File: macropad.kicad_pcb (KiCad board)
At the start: 2 copper layers, 187.7 x 88 mm, 79 parts, among them J1 SWD, J10 Keyboard 1, J11 Keyboard 1, J12 Keyboard 2, J13 Keyboard 2, J14 Keyboard 2, J15 Conn_01x12_Socket, J16 Conn_01x12_Pin, J2 Conn_01x12_Pin, J3 Conn_01x12_Socket, J4 Keyboard 1, J5 UART, J6 RS485, J7 Extra, J8 USB_A, J9 CAN, Q1 PNP, SW1 SW_Push, SW10 Reset, SW11 Reset, SW2 SW_Push, SW3 SW_Push, SW4 SW_Push, SW5 SW_Push, SW6 SW_Push, U1 AP62250WU, U2 STM32F042K6Tx, U3 MAX490E, U4 MCP2551-I-SN

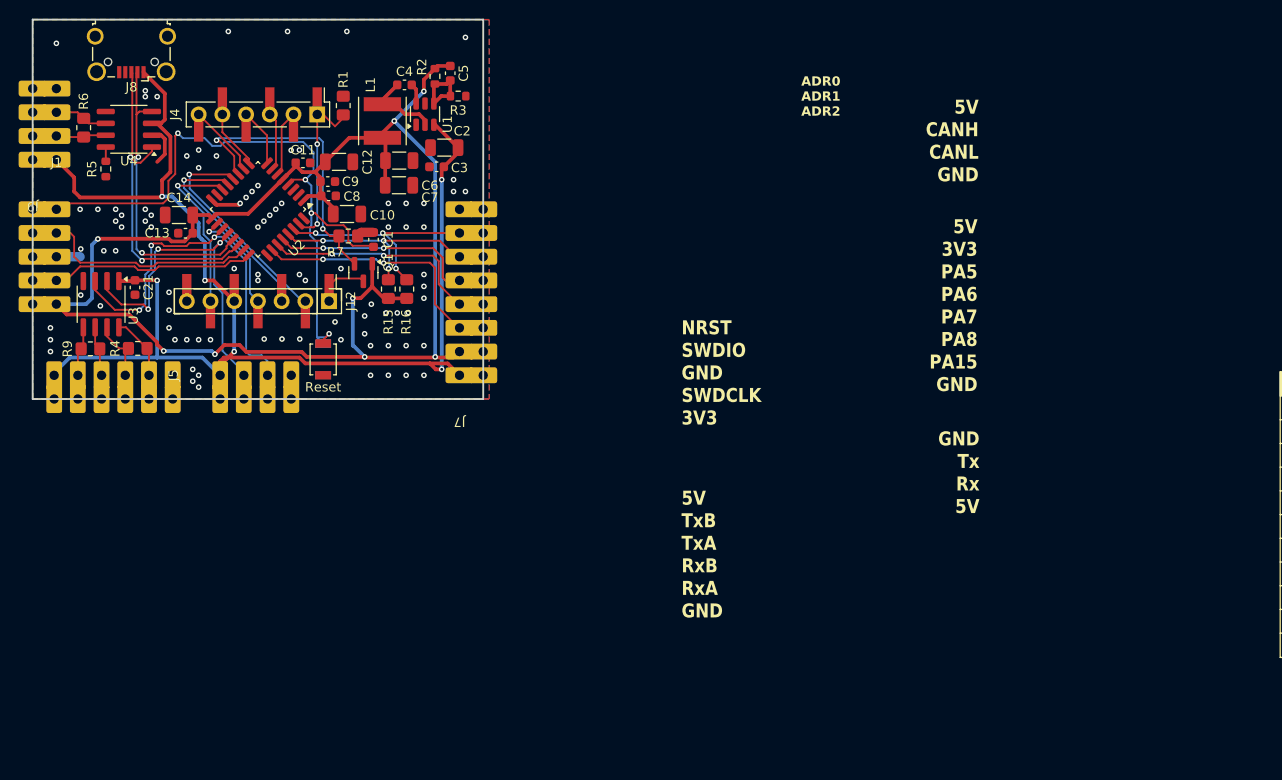
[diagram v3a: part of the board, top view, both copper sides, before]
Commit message: - fixed error in transistor circuit - fixed orientation of silkscreen text - DRC: Okay
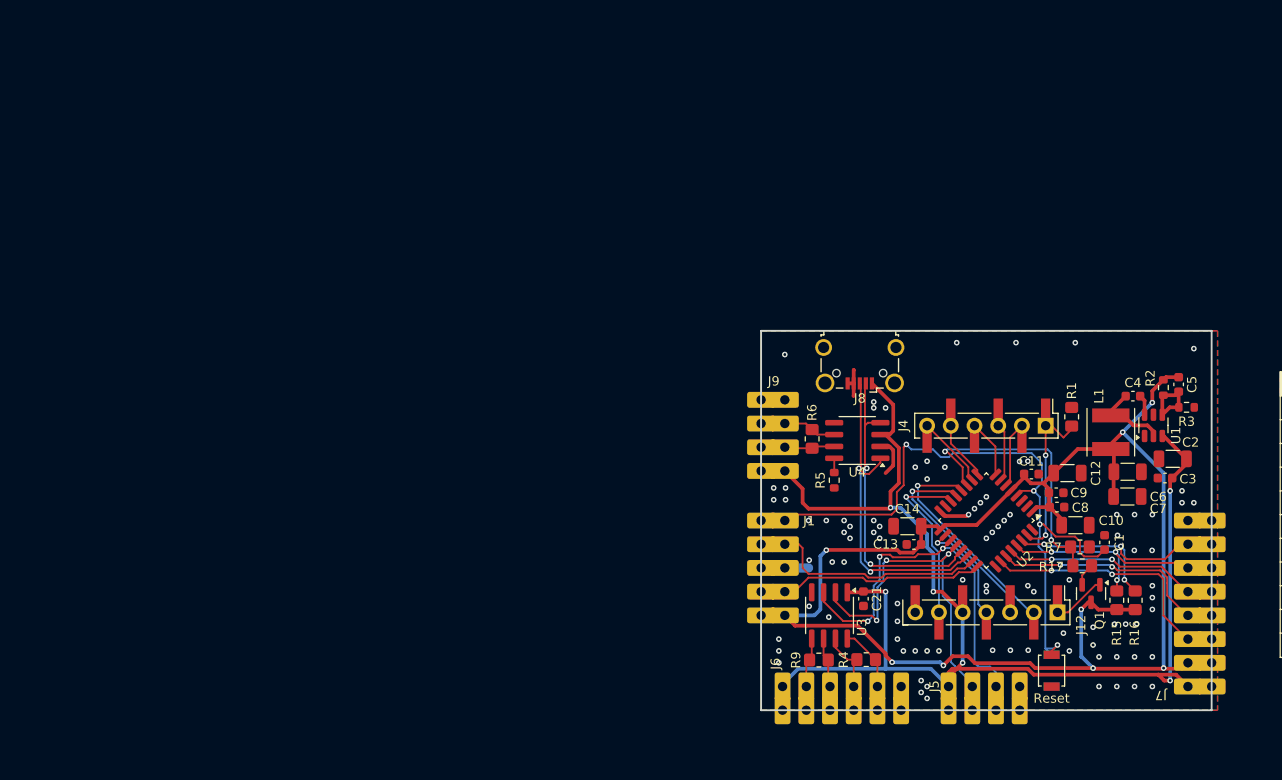
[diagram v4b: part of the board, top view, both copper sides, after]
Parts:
- added R17: 1k, Resistor_SMD:R_0805_2012Metric_Pad1.20x1.40mm_HandSolder, F.Cu at (126.3, 104.1)
- moved Q1 85.2 mm to (127.2, 107.1)
- moved R7 85.2 mm to (126.1, 102.1)
- moved C4 84.8 mm to (131.7, 86.0)
- moved J7 84.8 mm to (137.6, 117.1)
- moved R2 84.8 mm to (135.0, 85.0)
- moved U1 84.8 mm to (133.9, 89.1)
- moved C11 84.8 mm to (120.9, 94.3)
- moved C13 84.8 mm to (108.3, 101.9)
- moved C14 84.8 mm to (107.6, 99.9)
- moved C21 84.8 mm to (102.9, 107.7)
- moved C5 84.8 mm to (136.6, 84.7)
- moved C7 84.8 mm to (131.1, 96.7)
- moved C8 84.8 mm to (123.6, 97.9)
- moved J1 84.8 mm to (94.4, 99.3)
- moved J11 84.8 mm to (122.4, 89.1)
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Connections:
- Q1 pad 1: VDD -> GRP1
- Q1 pad 3: GRP1 -> VDD
- R7 pad 2: Net-(Q1-B) -> Net-(U2-PA5)
- U2 pad 11: Net-(Q1-B) -> Net-(U2-PA5)
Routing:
- net Net-(U2-PA5): track 0.00 -> 30.3 mm, vias 0 -> 2
- net Net-(Q1-B): track 31.9 -> 2.45 mm, vias 2 -> 0
- net VDD: track 163.1 -> 160.3 mm
- net GRP1: track 5.62 -> 7.26 mm
- net VSS: track 12.7 -> 14.3 mm, vias 89 -> 92
- net PB5: track 22.0 -> 20.7 mm
- net PB7: track 24.3 -> 25.2 mm
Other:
- board size 187.7 x 88 mm -> 109.7 x 70 mm
- board text added: "*CAN*"
- board text added: "*Extra* GND PB7 SDA PB6 SCL PB5 PB4 PB3 3V3 5V"
- board text added: "*PRG* NRST SWDIO GND SWDCLK 3V3"
- board text added: "*RS485*"
- board text added: "*UART*"
- board text added: "GND RxA RxB TxA TxB 5V"
- board text removed: "5V 3V3 PA5 PA6 PA7 PA8 PA15 GND"
- board text removed: "5V TxB TxA RxB RxA GND"
- board text removed: "ADR0 ADR1 ADR2"
- board text removed: "NRST SWDIO GND SWDCLK 3V3"

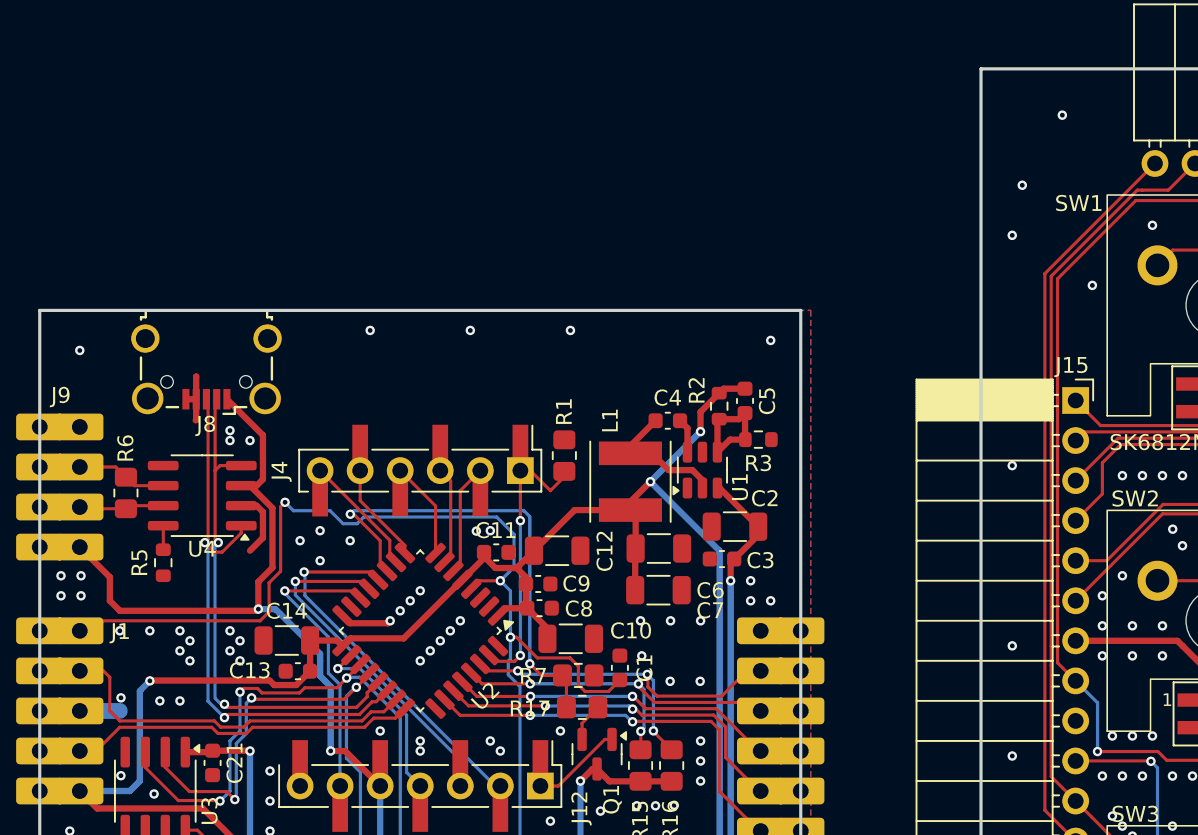
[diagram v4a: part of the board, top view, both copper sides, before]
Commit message: - Moved component name to silkscreen - Added version notation to boards
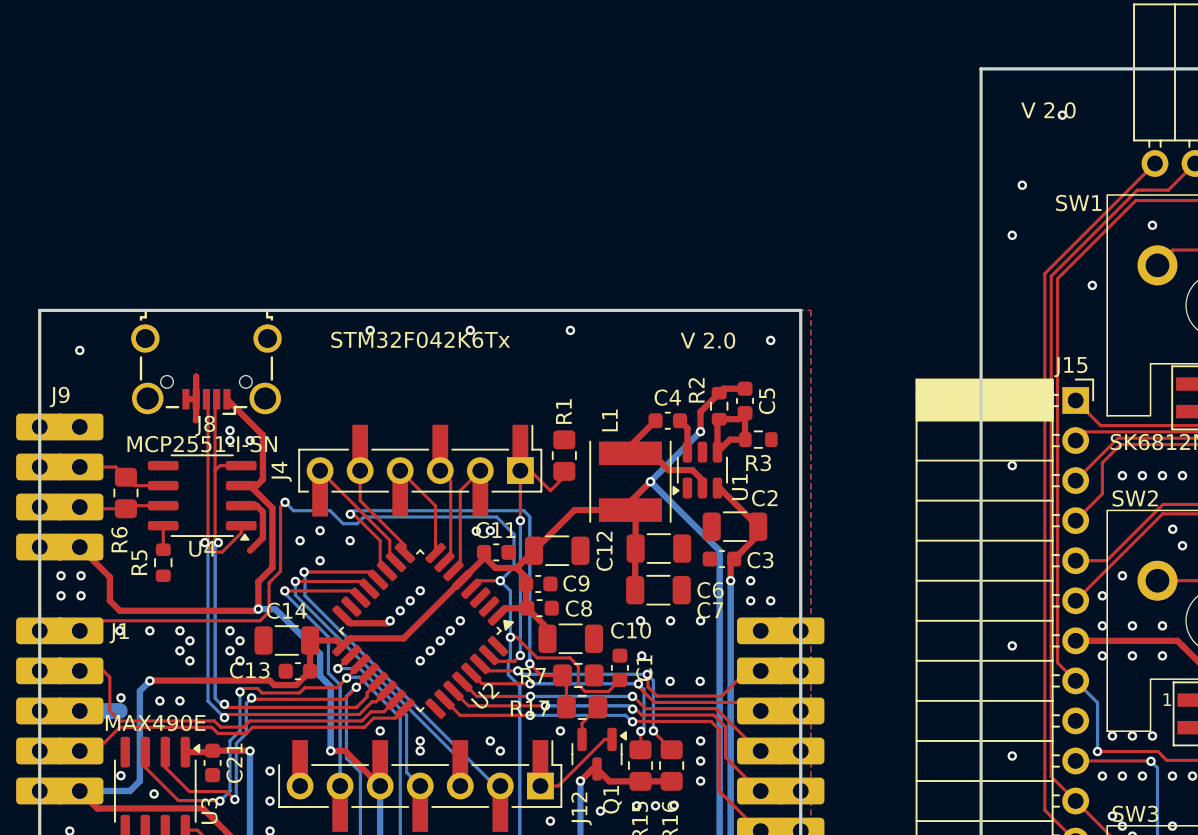
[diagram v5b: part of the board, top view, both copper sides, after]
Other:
- board text added: "V 2.0"
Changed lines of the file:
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@@
 		(allow_soldermask_bridges_in_footprints no)
 		(tenting front back)
-		(grid_origin 13.88 45.635)
+		(grid_origin 91.906177 78.971512)
 		(pcbplotparams
 			(layerselection 0x00000000_00000000_55555555_5755f5ff)
@@
 		(tags "resistor handsolder")
 		(property "Reference" "R6"
-			(at -2.829818 0 90)
+			(at 2.981145 0.374912 90)
 			(layer "F.SilkS")
 			(effects
@@
 		)
 		(property "Value" "STM32F042K6Tx"
-			(at 0 5.88 45)
-			(layer "F.Fab")
+			(at -13.021371 13.021371 0)
+			(layer "F.SilkS")
 			(effects
 				(font
@@
 		)
 		(property "Value" "MAX490E"
-			(at 0 3.4 90)
-			(layer "F.Fab")
+			(at -4.285371 0 180)
+			(layer "F.SilkS")
 			(effects
 				(font
@@
 		)
 		(property "Value" "MCP2551-I-SN"
-			(at 0 3.4 0)
-			(layer "F.Fab")
+			(at 0 3.231435 180)
+			(layer "F.SilkS")
 			(effects
 				(font
@@
 		(layer "Edge.Cuts")
 	)
+	(gr_text "V 2.0"
+		(at 154.136177 66.906512 0)
+		(layer "F.SilkS")
+		(effects
+			(font
+				(size 1 1)
+				(thickness 0.15)
+			)
+			(justify left bottom)
+		)
+	)
+	(gr_text "V 2.0"
+		(at 132.546177 81.511512 0)
+		(layer "F.SilkS")
+		(effects
+			(font
+				(size 1 1)
+				(thickness 0.15)
+			)
+			(justify left bottom)
+		)
+	)
 	(gr_text "\n5V\nCANH\nCANL\nGND"

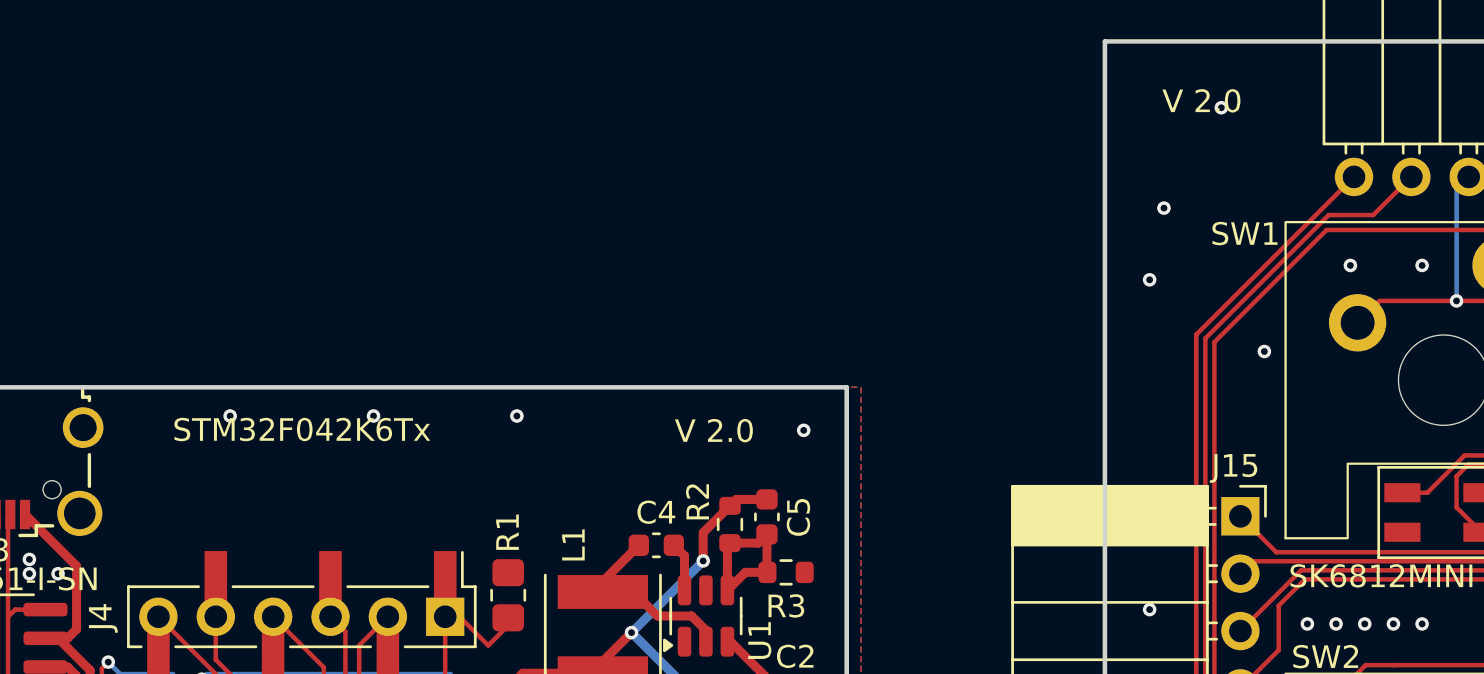
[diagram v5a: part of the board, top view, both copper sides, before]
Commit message: - Added missing library files to git - Added logo to silkscreen - ERC: Okay
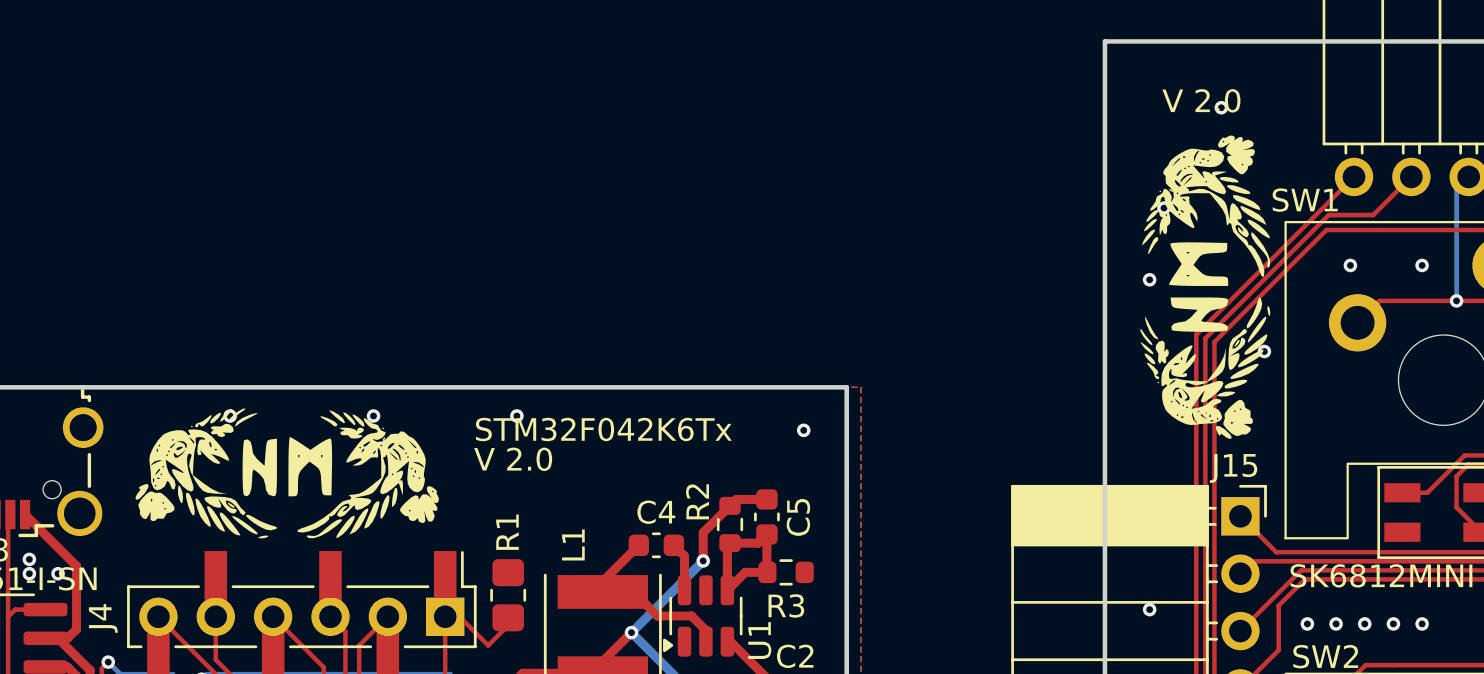
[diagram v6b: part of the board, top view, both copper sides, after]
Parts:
- added G***: LOGO, LOGO, F.Cu at (115.4, 82.8)
- added G***: LOGO, LOGO, F.Cu at (156.0, 74.5)
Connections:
- net USART1_RX renamed USART1_Rx
- net USART1_TX renamed USART1_Tx

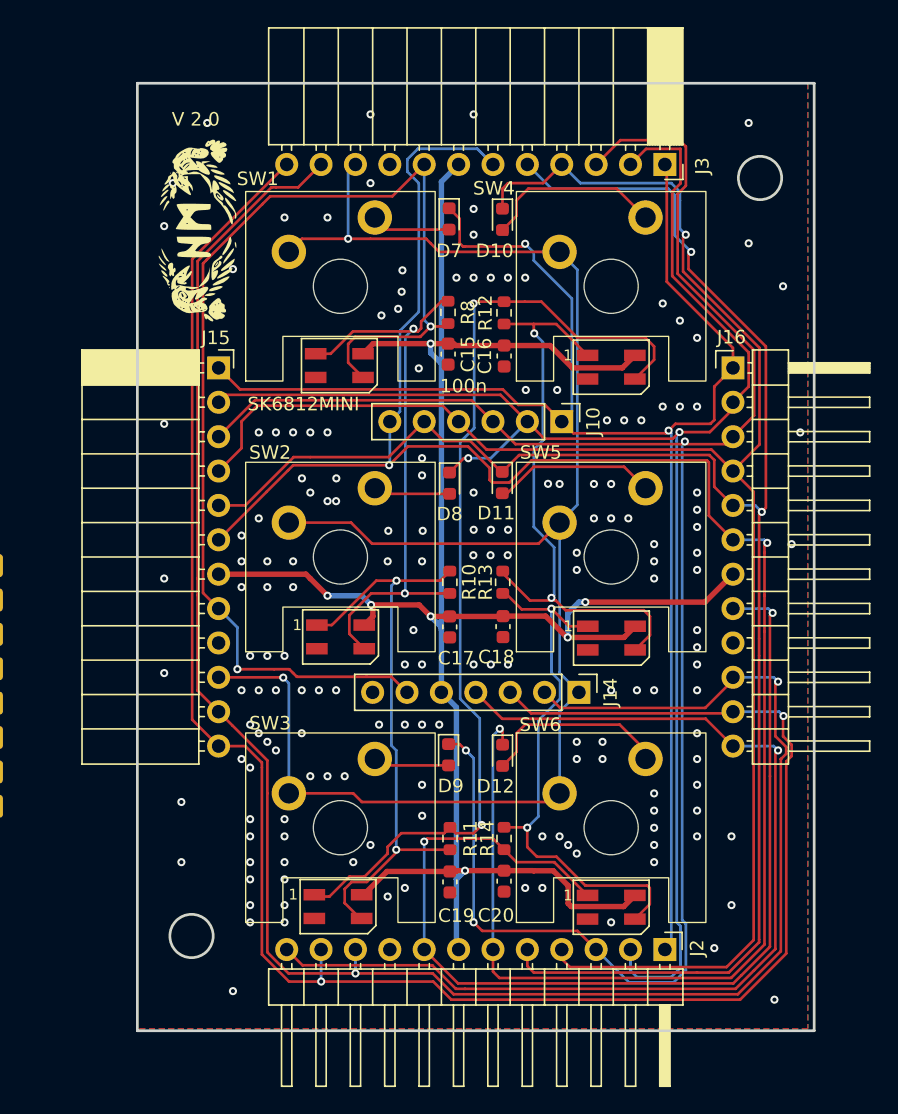
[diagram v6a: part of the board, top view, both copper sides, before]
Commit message: Separated Keyboard schematic and pcb to a separate project in the same folder.
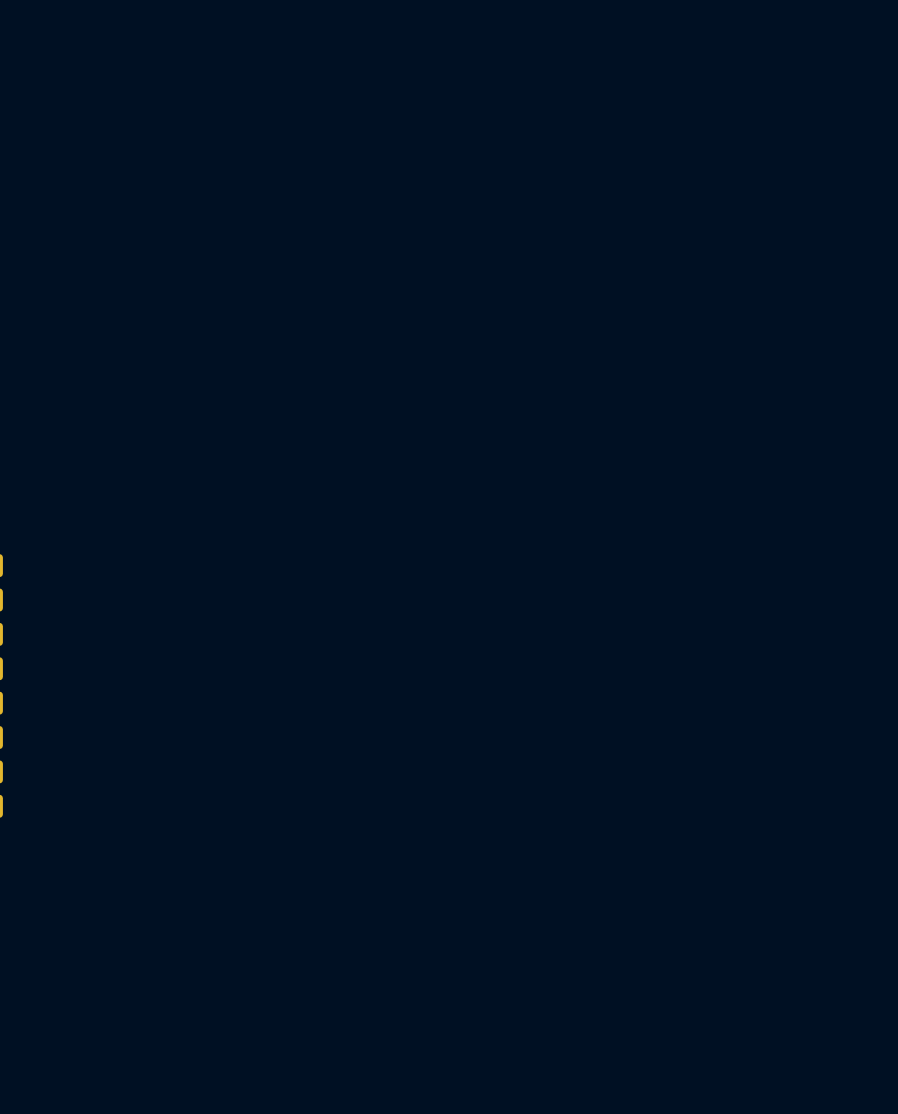
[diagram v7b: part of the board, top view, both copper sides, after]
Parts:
- removed C15, C16, C17, C18, C19, C20: 100n, Capacitor_SMD:C_0603_1608Metric
- removed D1, D2, D3, D4, D5, D6: SK6812MINI, LED_SMD:LED_SK6812MINI_PLCC4_3.5x3.5mm_P1.75mm
- removed D10, D11, D12, D7, D8, D9: D, Diode_SMD:D_0603_1608Metric
- removed the G*** at (156.0, 74.5)
- removed J10: Keyboard 1, Connector_PinHeader_2.54mm:PinHeader_1x06_P2.54mm_Vertical
- removed J14: Keyboard 2, Connector_PinHeader_2.54mm:PinHeader_1x07_P2.54mm_Vertical
- removed J15, J3: Conn_01x12_Socket, Connector_PinSocket_2.54mm:PinSocket_1x12_P2.54mm_Horizontal
- removed J16, J2: Conn_01x12_Pin, Connector_PinHeader_2.54mm:PinHeader_1x12_P2.54mm_Horizontal
- removed R10, R11, R12, R13, R14, R8: R, Resistor_SMD:R_0603_1608Metric
- removed SW1, SW2, SW3, SW4, SW5, SW6: SW_Push, Button_Switch_Keyboard:Gateron Pro
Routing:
- net +5V #2: track 157.9 -> 0.00 mm, vias 7 -> 0
- net H_BTN6: track 152.2 -> 0.00 mm, vias 3 -> 0
- net H_GRP3: track 147.5 -> 0.00 mm, vias 2 -> 0
- net H_GRP2: track 146.8 -> 0.00 mm, vias 2 -> 0
- net H_BTN3: track 144.5 -> 0.00 mm, vias 3 -> 0
- net H_BTN5: track 137.3 -> 0.00 mm, vias 2 -> 0
- net H_BTN4: track 134.6 -> 0.00 mm, vias 1 -> 0
- net H_GRP1: track 125.0 -> 0.00 mm, vias 2 -> 0
- net H_BTN1: track 122.4 -> 0.00 mm, vias 2 -> 0
- net H_BTN2: track 119.9 -> 0.00 mm, vias 2 -> 0
- net LED_DATA_IN: track 86.7 -> 0.00 mm, vias 2 -> 0
- net H_GRP4: track 77.4 -> 0.00 mm, vias 1 -> 0
- net LED_DATA_OUT: track 77.4 -> 0.00 mm, vias 2 -> 0
- net Net-(D3-DOUT): track 73.0 -> 0.00 mm, vias 2 -> 0
- net Net-(D4-DOUT): track 43.9 -> 0.00 mm, vias 2 -> 0
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- removed copper zone on B.Cu, net GND #2
- removed copper zone on F.Cu, net GND #2
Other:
- board size 109.7 x 70 mm -> 48.3 x 40.6 mm
